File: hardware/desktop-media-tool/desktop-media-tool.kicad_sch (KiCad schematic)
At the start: 0 parts

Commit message: Usb hid device test
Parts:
- added J1: Conn_01x08_Socket, symbol Conn_01x08_Socket:Conn_01x08_Socket
- added SW1: RotaryEncoder_Switch, symbol RotaryEncoder_Switch:RotaryEncoder_Switch
- added XMEGA1: XMEGABoard-Rev1.11, symbol hva:XMEGABoard-Rev1.11

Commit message: Shematic edit
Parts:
- removed XMEGA1: XMEGABoard-Rev1.11, symbol hva:XMEGABoard-Rev1.11
- added IC1: ATXMEGA256A3U-MH, QFN50P900X900X100-65N-D, symbol ATXMEGA256A3U-MH:ATXMEGA256A3U-MH
- added P1: USB_C_Plug_USB2.0, symbol USB_C_Plug_USB2.0:USB_C_Plug_USB2.0
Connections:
- new net: P1.A1 (GND), P1.A12 (GND), P1.B1 (GND), P1.B12 (GND)
- new net: P1.A4 (VBUS), P1.A9 (VBUS), P1.B4 (VBUS), P1.B9 (VBUS)

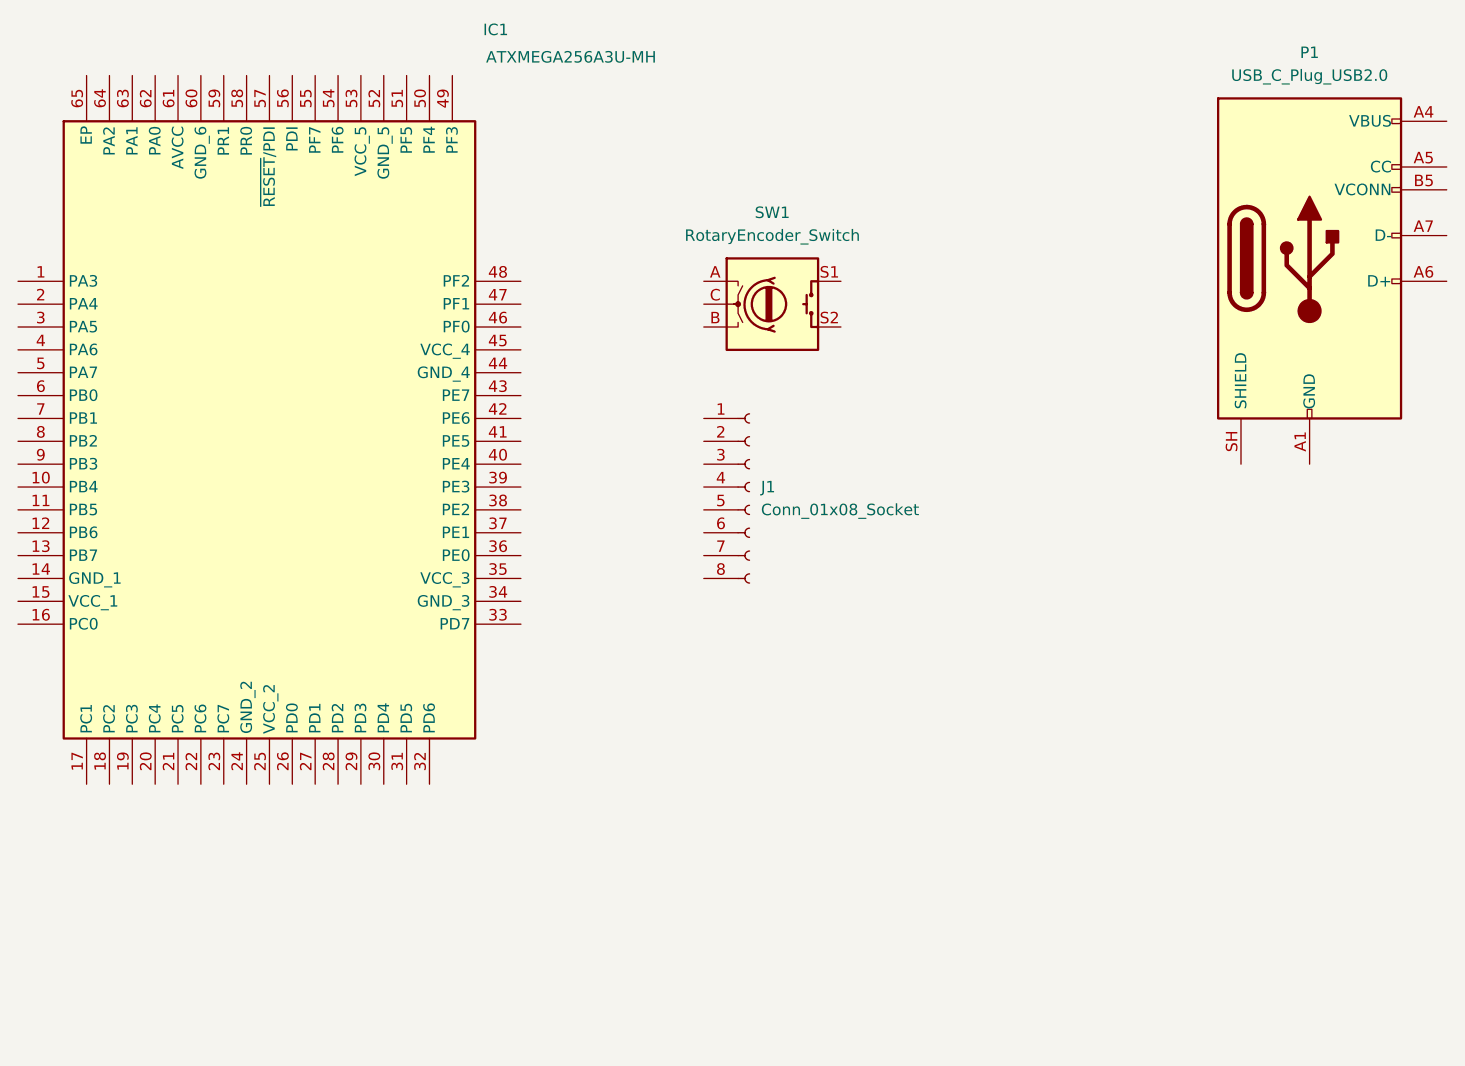
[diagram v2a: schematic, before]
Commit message: Decoupling caps
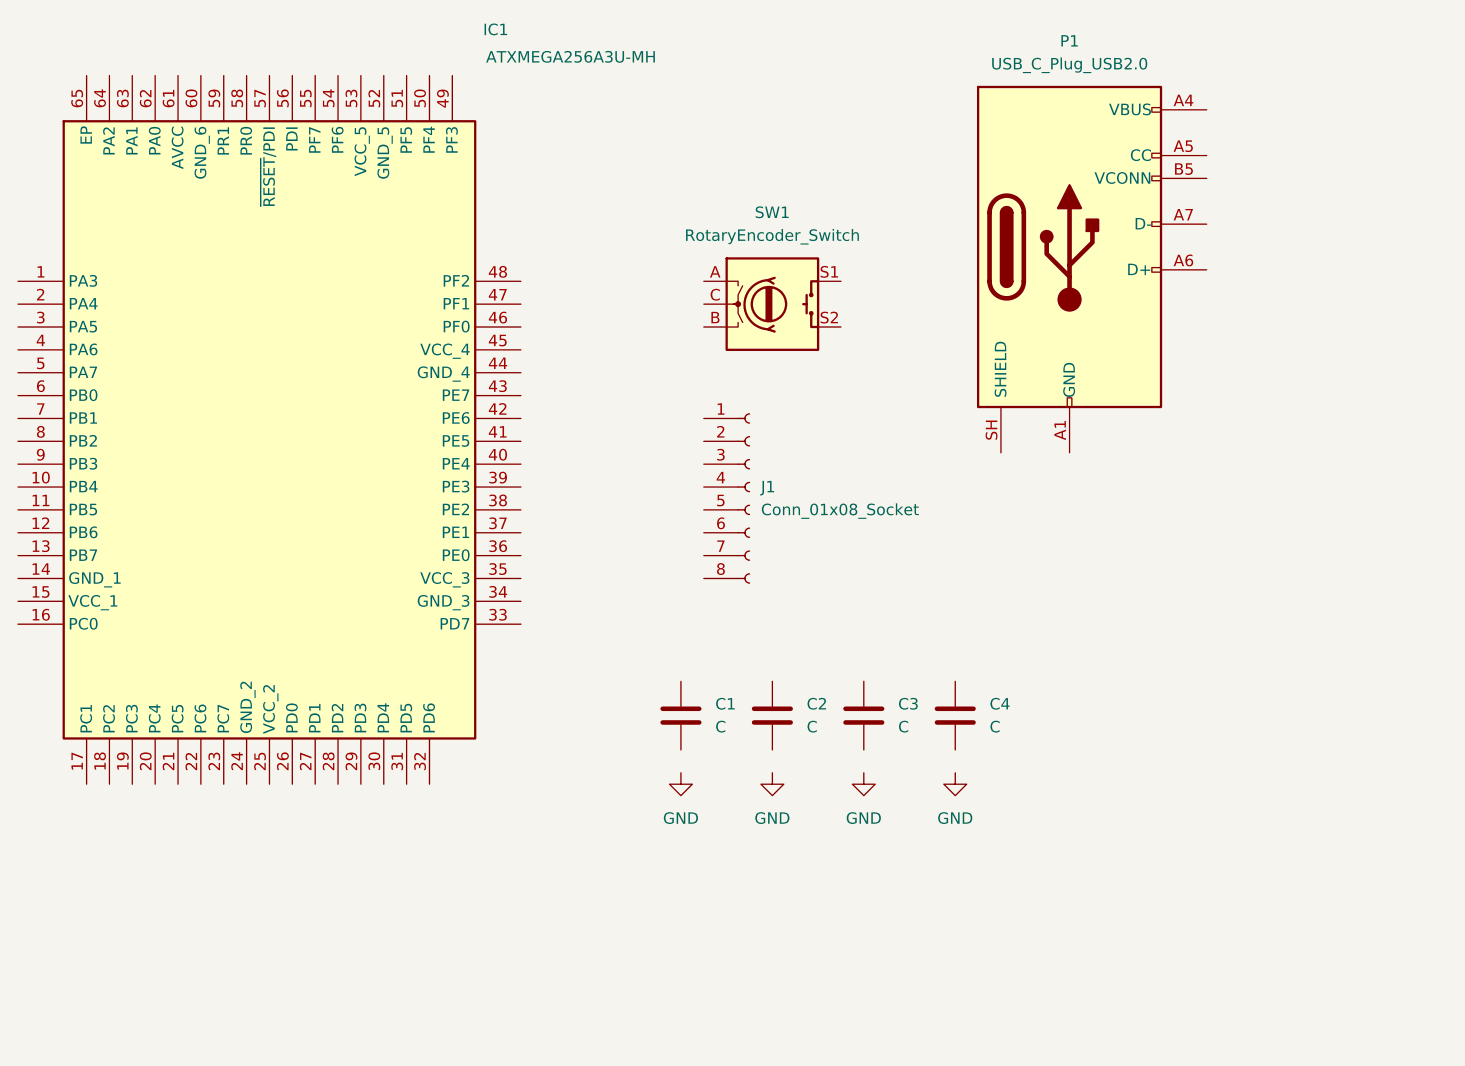
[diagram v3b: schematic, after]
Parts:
- added C1, C2, C3, C4: C, symbol C:C
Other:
- moved on the sheet: P1
